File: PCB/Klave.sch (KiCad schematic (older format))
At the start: 77 parts, among them J2 OLED, SW0 Reset, SW1 0:0, SW10 1:3, SW11 1:4, SW12 1:5, SW13 2:0, SW14 2:1, SW15 2:2, SW16 2:3, SW17 2:4, SW18 2:5, SW19 3:0, SW2 0:1, SW20 3:1, SW21 3:2, SW22 3:3, SW23 3:4, SW24 3:5, SW26 4:1, SW27 4:2, SW28 4:3, SW29 4:4, SW3 0:2, SW30 4:5, SW31 5:0, SW35 5:4, SW36 5:5, SW4 0:3, SW5 0:4, SW6 0:5, SW7 1:0, SW8 1:1, SW9 1:2, U1 ProMicro

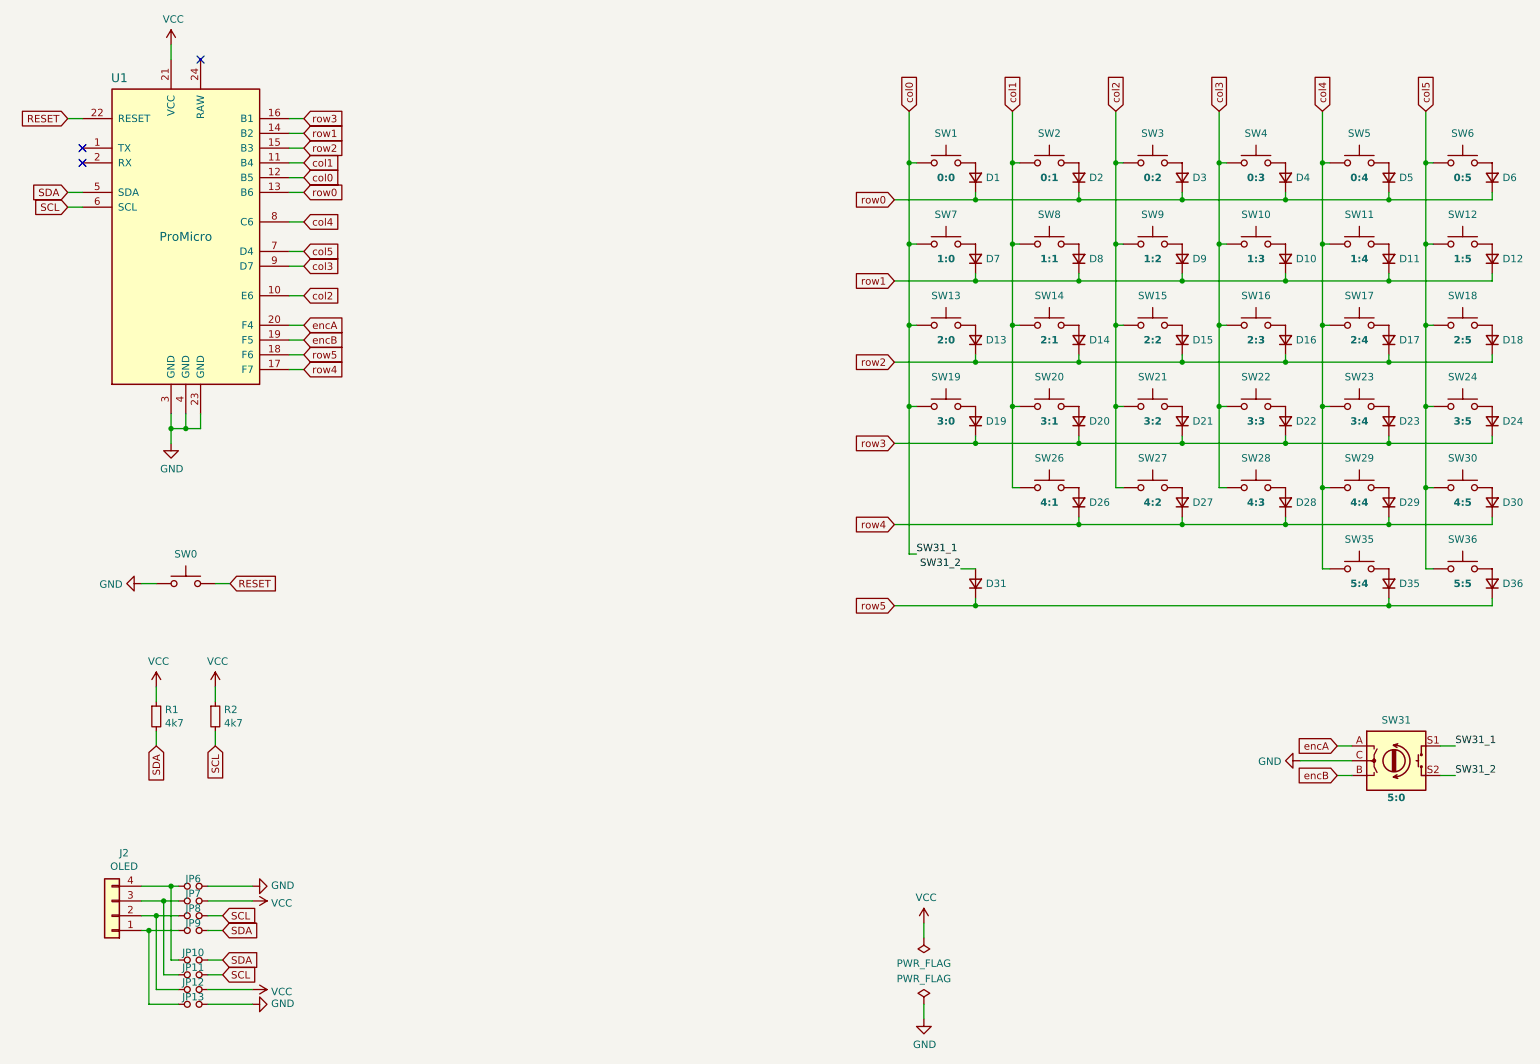
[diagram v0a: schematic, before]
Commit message: Add RJ12 schematic symbol and footprint
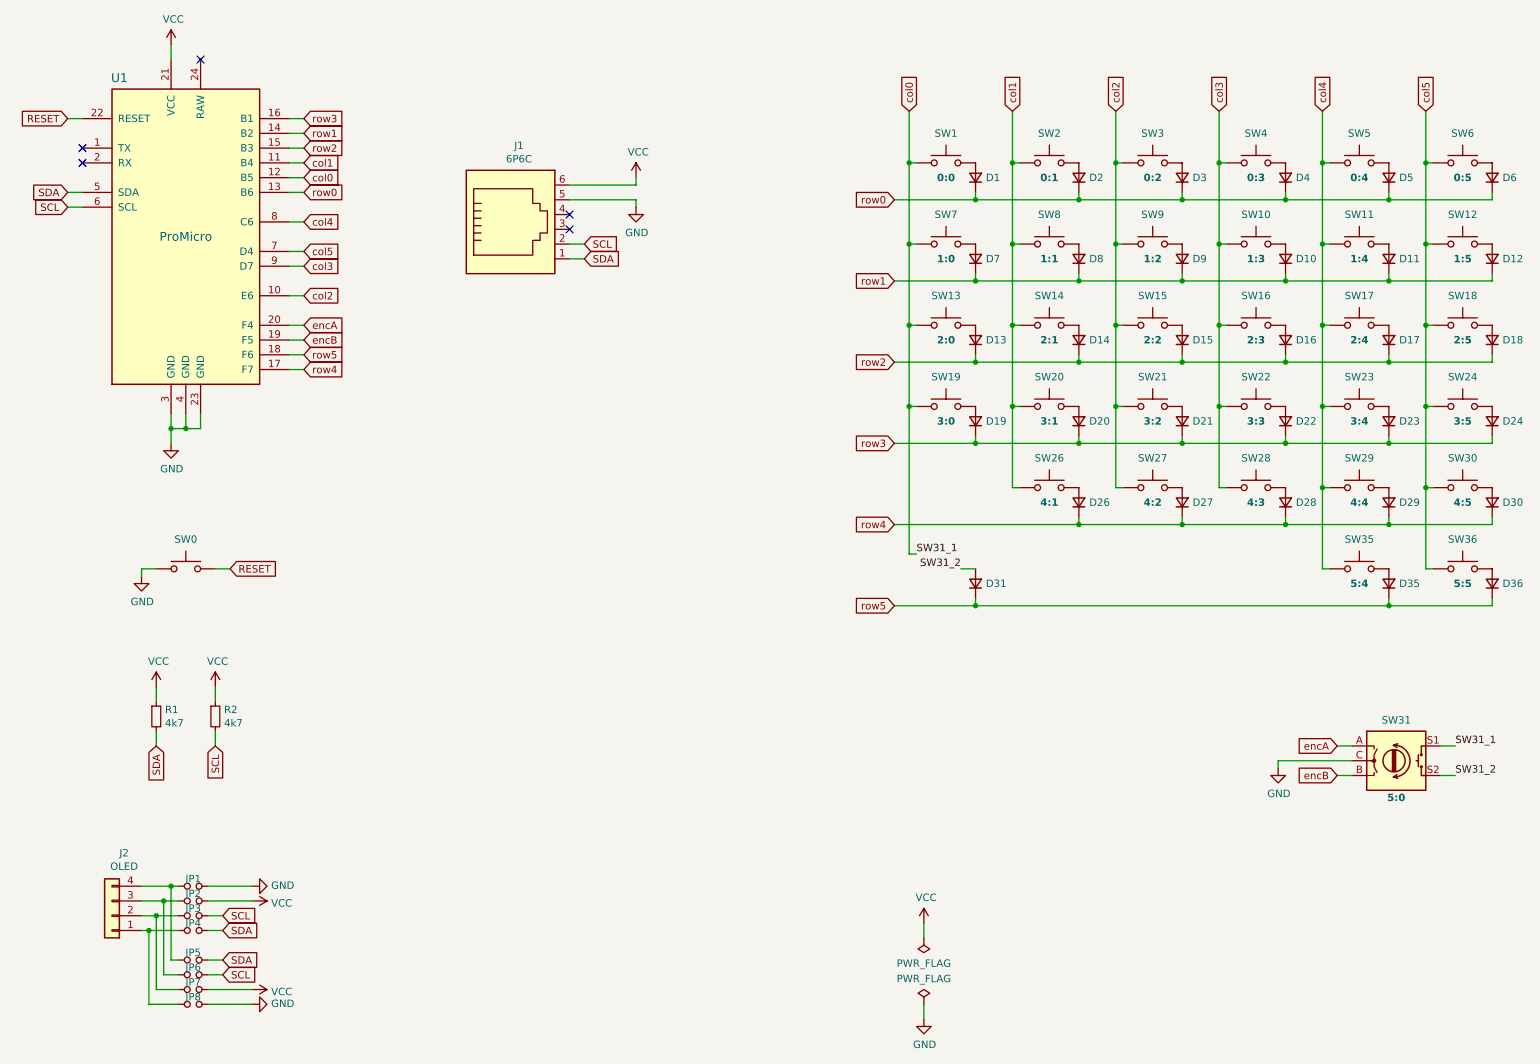
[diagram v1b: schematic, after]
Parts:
- added J1: 6P6C, KlaveLib:RJ12_6P6C, symbol Connector:6P6C
- renumbered JP6 to JP1, JP7 to JP2, JP8 to JP3, JP9 to JP4, JP10 to JP5, JP11 to JP6, JP12 to JP7, JP13 to JP8
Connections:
- net GND: now also J1.5
- net SCL: now also J1.2
- net SDA: now also J1.1
- net VCC: now also J1.6
- no-connect marks 3 -> 5
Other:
- moved on the sheet: SW0
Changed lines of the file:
@@
 Comment4 ""
 $EndDescr
-$Comp
-L Connector_Generic:Conn_01x04 J2
-U 1 1 5F4351F9
-P 1200 6800
-F 0 "J2" H 1118 6375 50  0000 C CNN
-F 1 "OLED" H 1118 6466 50  0000 C CNN
-F 2 "KlaveLib:Display_OLED_128x32" H 1200 6800 50  0001 C CNN
-F 3 "~" H 1200 6800 50  0001 C CNN
-	1    1200 6800
-	-1   0    0    1
-$EndComp
 Text GLabel 900  1400 0    50   Input ~ 0
 RESET
@@
 L Switch:SW_Push SW0
 U 1 1 5F45BBB3
-P 1700 4550
-F 0 "SW0" H 1700 4750 50  0000 C CNN
-F 1 "Reset" H 1700 4744 50  0001 C CNN
-F 2 "KlaveLib:SW_Tactile_2pin" H 1700 4750 50  0001 C CNN
-F 3 "~" H 1700 4750 50  0001 C CNN
-	1    1700 4550
-	1    0    0    -1
-$EndComp
-$Comp
-L power:GND #PWR0108
-U 1 1 5F45DA69
-P 1400 4550
-F 0 "#PWR0108" H 1400 4300 50  0001 C CNN
-F 1 "GND" V 1405 4422 50  0000 R CNN
-F 2 "" H 1400 4550 50  0001 C CNN
-F 3 "" H 1400 4550 50  0001 C CNN
-	1    1400 4550
-	0    1    1    0
-$EndComp
-Text GLabel 2000 4550 2    50   Input ~ 0
+P 1700 4450
+F 0 "SW0" H 1700 4650 50  0000 C CNN
+F 1 "Reset" H 1700 4644 50  0001 C CNN
+F 2 "KlaveLib:SW_Tactile_2pin" H 1700 4650 50  0001 C CNN
+F 3 "~" H 1700 4650 50  0001 C CNN
+	1    1700 4450
+	1    0    0    -1
+$EndComp
+Text GLabel 2000 4450 2    50   Input ~ 0
 RESET
 Wire Wire Line
-	1900 4550 2000 4550
-Wire Wire Line
-	1400 4550 1500 4550
+	1900 4450 2000 4450
+Wire Wire Line
+	1400 4450 1500 4450
 Wire Wire Line
 	900  2000 1000 2000
@@
 	1000 1400 900  1400
 $Comp
-L Device:Jumper_NO_Small JP6
+L Device:Jumper_NO_Small JP1
 U 1 1 5F4432FB
 P 1750 6600
-F 0 "JP6" H 1750 6650 50  0000 C CNN
+F 0 "JP1" H 1750 6650 50  0000 C CNN
 F 1 "Front" H 1750 6694 50  0001 C CNN
 F 2 "Jumper:SolderJumper-2_P1.3mm_Open_Pad1.0x1.5mm" H 1750 6600 50  0001 C CNN
@@
 $EndComp
 $Comp
-L Device:Jumper_NO_Small JP7
+L Device:Jumper_NO_Small JP2
 U 1 1 5F44580E
 P 1750 6700
-F 0 "JP7" H 1750 6750 50  0000 C CNN
+F 0 "JP2" H 1750 6750 50  0000 C CNN
 F 1 "Front" H 1750 6794 50  0001 C CNN
 F 2 "Jumper:SolderJumper-2_P1.3mm_Open_Pad1.0x1.5mm" H 1750 6700 50  0001 C CNN
@@
 $EndComp
 $Comp
-L Device:Jumper_NO_Small JP8
+L Device:Jumper_NO_Small JP3
 U 1 1 5F445A8A
 P 1750 6800
-F 0 "JP8" H 1750 6850 50  0000 C CNN
+F 0 "JP3" H 1750 6850 50  0000 C CNN
 F 1 "Front" H 1750 6894 50  0001 C CNN
 F 2 "Jumper:SolderJumper-2_P1.3mm_Open_Pad1.0x1.5mm" H 1750 6800 50  0001 C CNN
@@
 $EndComp
 $Comp
-L Device:Jumper_NO_Small JP9
+L Device:Jumper_NO_Small JP4
 U 1 1 5F445CFD
 P 1750 6900
-F 0 "JP9" H 1750 6950 50  0000 C CNN
+F 0 "JP4" H 1750 6950 50  0000 C CNN
 F 1 "Front" H 1750 6994 50  0001 C CNN
 F 2 "Jumper:SolderJumper-2_P1.3mm_Open_Pad1.0x1.5mm" H 1750 6900 50  0001 C CNN
@@
 	1850 6900 1950 6900
 $Comp
-L Device:Jumper_NO_Small JP10
+L Device:Jumper_NO_Small JP5
 U 1 1 5F44AC54
 P 1750 7100
-F 0 "JP10" H 1750 7150 50  0000 C CNN
+F 0 "JP5" H 1750 7150 50  0000 C CNN
 F 1 "Back" H 1750 7194 50  0001 C CNN
 F 2 "Jumper:SolderJumper-2_P1.3mm_Open_Pad1.0x1.5mm" H 1750 7100 50  0001 C CNN
@@
 $EndComp
 $Comp
-L Device:Jumper_NO_Small JP11
+L Device:Jumper_NO_Small JP6
 U 1 1 5F44B03B
 P 1750 7200
-F 0 "JP11" H 1750 7250 50  0000 C CNN
+F 0 "JP6" H 1750 7250 50  0000 C CNN
 F 1 "Back" H 1750 7294 50  0001 C CNN
 F 2 "Jumper:SolderJumper-2_P1.3mm_Open_Pad1.0x1.5mm" H 1750 7200 50  0001 C CNN
@@
 	6600 4350 6600 3350
 Connection ~ 6600 3350
-$Comp
-L power:GND #PWR0115
-U 1 1 5F686B26
-P 9250 5750
-F 0 "#PWR0115" H 9250 5500 50  0001 C CNN
-F 1 "GND" V 9255 5622 50  0000 R CNN
-F 2 "" H 9250 5750 50  0001 C CNN
-F 3 "" H 9250 5750 50  0001 C CNN
-	1    9250 5750
-	0    1    1    0
-$EndComp
-Wire Wire Line
-	9600 5750 9250 5750
 Text GLabel 9500 5850 0    50   Input ~ 0
 encB
@@
 	2500 3000 2400 3000
 $Comp
-L Device:Jumper_NO_Small JP12
+L Device:Jumper_NO_Small JP7
 U 1 1 5F44B29F
 P 1750 7300
-F 0 "JP12" H 1750 7350 50  0000 C CNN
+F 0 "JP7" H 1750 7350 50  0000 C CNN
 F 1 "Back" H 1750 7394 50  0001 C CNN
 F 2 "Jumper:SolderJumper-2_P1.3mm_Open_Pad1.0x1.5mm" H 1750 7300 50  0001 C CNN
@@
 $EndComp
 $Comp
-L Device:Jumper_NO_Small JP13
+L Device:Jumper_NO_Small JP8
 U 1 1 5F44B531
 P 1750 7400
-F 0 "JP13" H 1750 7450 50  0000 C CNN
+F 0 "JP8" H 1750 7450 50  0000 C CNN
 F 1 "Back" H 1750 7494 50  0001 C CNN
 F 2 "Jumper:SolderJumper-2_P1.3mm_Open_Pad1.0x1.5mm" H 1750 7400 50  0001 C CNN
@@
 	1    0    0    -1
 $EndComp
+$Comp
+L Connector:6P6C J1
+U 1 1 5F4F184F
+P 3900 2150
+F 0 "J1" H 3957 2717 50  0000 C CNN
+F 1 "6P6C" H 3957 2626 50  0000 C CNN
+F 2 "KlaveLib:RJ12_6P6C" V 3900 2175 50  0001 C CNN
+F 3 "~" V 3900 2175 50  0001 C CNN
+	1    3900 2150
+	1    0    0    -1
+$EndComp
+Text GLabel 4400 2250 2    50   Input ~ 0
+SCL
+Text GLabel 4400 2350 2    50   Input ~ 0
+SDA
+Wire Wire Line
+	4300 2250 4400 2250
+Wire Wire Line
+	4300 2350 4400 2350
+NoConn ~ 4300 2150
+NoConn ~ 4300 2050
+Wire Wire Line
+	4300 1950 4750 1950
+Wire Wire Line
+	4750 1950 4750 2000
+Wire Wire Line
+	4300 1850 4750 1850
+Wire Wire Line
+	4750 1850 4750 1800
+$Comp
+L power:GND #PWR?
+U 1 1 5F5CB4B4
+P 4750 2000
+F 0 "#PWR?" H 4750 1750 50  0001 C CNN
+F 1 "GND" H 4755 1827 50  0000 C CNN
+F 2 "" H 4750 2000 50  0001 C CNN
+F 3 "" H 4750 2000 50  0001 C CNN
+	1    4750 2000
+	1    0    0    -1
+$EndComp
+$Comp
+L power:VCC #PWR?
+U 1 1 5F5CA8C4
+P 4750 1800
+F 0 "#PWR?" H 4750 1650 50  0001 C CNN
+F 1 "VCC" H 4765 1973 50  0000 C CNN
+F 2 "" H 4750 1800 50  0001 C CNN
+F 3 "" H 4750 1800 50  0001 C CNN
+	1    4750 1800
+	1    0    0    -1
+$EndComp
+$Comp
+L Connector_Generic:Conn_01x04 J2
+U 1 1 5F4351F9
+P 1200 6800
+F 0 "J2" H 1118 6375 50  0000 C CNN
+F 1 "OLED" H 1118 6466 50  0000 C CNN
+F 2 "KlaveLib:Display_OLED_128x32" H 1200 6800 50  0001 C CNN
+F 3 "~" H 1200 6800 50  0001 C CNN
+	1    1200 6800
+	-1   0    0    1
+$EndComp
+$Comp
+L power:GND #PWR?
+U 1 1 5F62CBB5
+P 1400 4500
+F 0 "#PWR?" H 1400 4250 50  0001 C CNN
+F 1 "GND" H 1405 4327 50  0000 C CNN
+F 2 "" H 1400 4500 50  0001 C CNN
+F 3 "" H 1400 4500 50  0001 C CNN
+	1    1400 4500
+	1    0    0    -1
+$EndComp
+Wire Wire Line
+	1400 4450 1400 4500
+$Comp
+L power:GND #PWR?
+U 1 1 5F64CA49
+P 9100 5800
+F 0 "#PWR?" H 9100 5550 50  0001 C CNN
+F 1 "GND" H 9105 5627 50  0000 C CNN
+F 2 "" H 9100 5800 50  0001 C CNN
+F 3 "" H 9100 5800 50  0001 C CNN
+	1    9100 5800
+	1    0    0    -1
+$EndComp
+Wire Wire Line
+	9100 5750 9600 5750
+Wire Wire Line
+	9100 5800 9100 5750
 $EndSCHEMATC

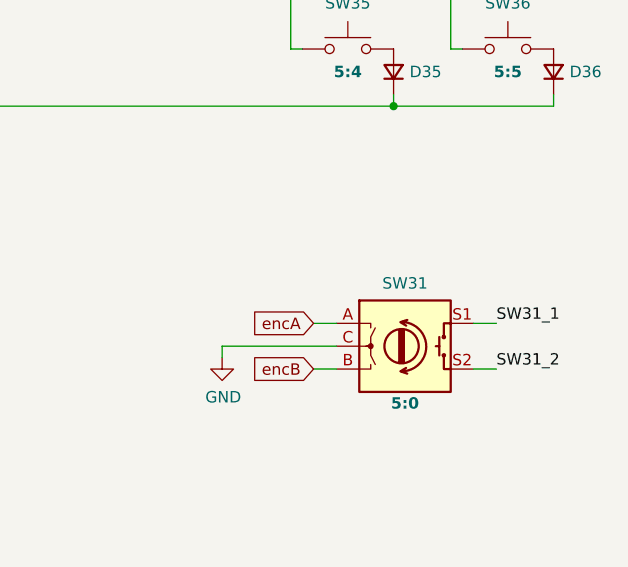
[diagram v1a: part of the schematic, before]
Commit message: Change rotary encoder reference name from SW to ENC
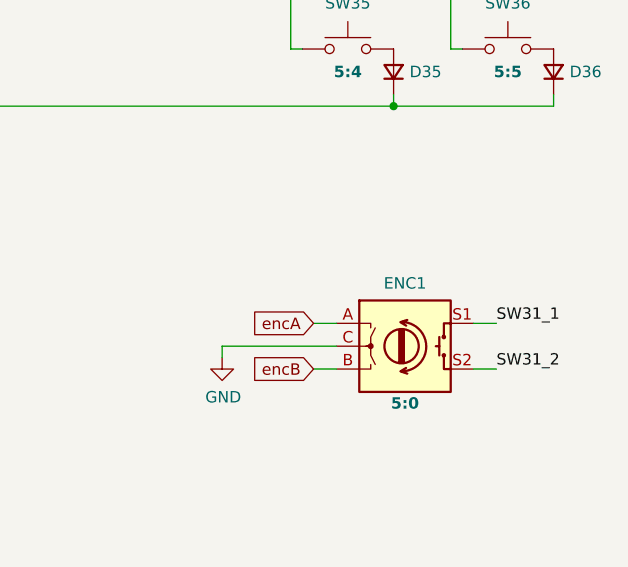
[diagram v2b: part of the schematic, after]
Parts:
- renumbered SW31 to ENC1
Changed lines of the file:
@@
 	6500 4700 7050 4700
 $Comp
-L Device:Rotary_Encoder_Switch SW31
+L Device:Rotary_Encoder_Switch ENC1
 U 1 1 5F65CF2A
 P 9900 5750
-F 0 "SW31" H 9900 6025 50  0000 C CNN
+F 0 "ENC1" H 9900 6025 50  0000 C CNN
 F 1 "5:0" H 9900 5500 50  0000 C CNB
 F 2 "KlaveLib:RotaryEncoder_EC11E-Switch" H 9750 5910 50  0001 C CNN
@@
 	4750 1850 4750 1800
 $Comp
-L power:GND #PWR?
+L power:GND #PWR0103
 U 1 1 5F5CB4B4
 P 4750 2000
-F 0 "#PWR?" H 4750 1750 50  0001 C CNN
+F 0 "#PWR0103" H 4750 1750 50  0001 C CNN
 F 1 "GND" H 4755 1827 50  0000 C CNN
 F 2 "" H 4750 2000 50  0001 C CNN
@@
 $EndComp
 $Comp
-L power:VCC #PWR?
+L power:VCC #PWR0104
 U 1 1 5F5CA8C4
 P 4750 1800
-F 0 "#PWR?" H 4750 1650 50  0001 C CNN
+F 0 "#PWR0104" H 4750 1650 50  0001 C CNN
 F 1 "VCC" H 4765 1973 50  0000 C CNN
 F 2 "" H 4750 1800 50  0001 C CNN
@@
 $EndComp
 $Comp
-L power:GND #PWR?
+L power:GND #PWR0105
 U 1 1 5F62CBB5
 P 1400 4500
-F 0 "#PWR?" H 1400 4250 50  0001 C CNN
+F 0 "#PWR0105" H 1400 4250 50  0001 C CNN
 F 1 "GND" H 1405 4327 50  0000 C CNN
 F 2 "" H 1400 4500 50  0001 C CNN
@@
 	1400 4450 1400 4500
 $Comp
-L power:GND #PWR?
+L power:GND #PWR0108
 U 1 1 5F64CA49
 P 9100 5800
-F 0 "#PWR?" H 9100 5550 50  0001 C CNN
+F 0 "#PWR0108" H 9100 5550 50  0001 C CNN
 F 1 "GND" H 9105 5627 50  0000 C CNN
 F 2 "" H 9100 5800 50  0001 C CNN
